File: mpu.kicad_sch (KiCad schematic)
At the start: 14 parts, among them IC1 MC6809E, J18 RESET

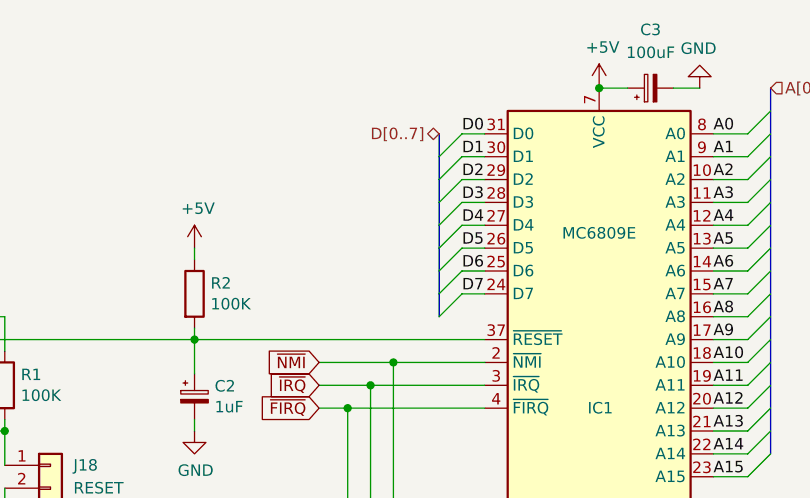
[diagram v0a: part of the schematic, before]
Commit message: add data bus transceiver
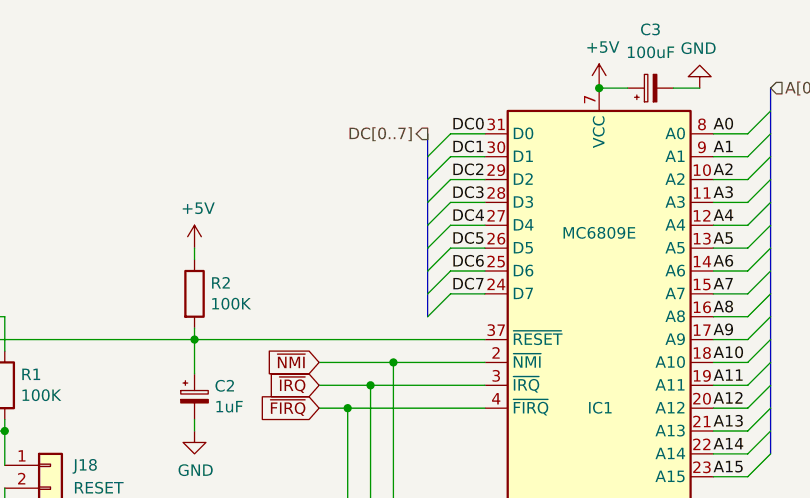
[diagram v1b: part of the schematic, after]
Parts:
- C1: DigiKey BC1101CT-ND -> 399-C0805C104K4RAC7800CT-ND
- C3: DigiKey 732-8598-1-ND -> 732-6410-1-ND
- R1, R2: DigiKey CF14JT100KCT-ND -> 738-RNCF0805DTE100KCT-ND
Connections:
- net D0 renamed DC0
- net D1 renamed DC1
- net D2 renamed DC2
- net D3 renamed DC3
- net D4 renamed DC4
- net D5 renamed DC5
- net D6 renamed DC6
- net D7 renamed DC7
